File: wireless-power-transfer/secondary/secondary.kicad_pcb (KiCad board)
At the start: 2 copper layers, 100 x 67 mm, 9 parts, among them J1 Screw_Terminal_1x02, J2 Screw_Terminal_1x02, U1 LM7812CT

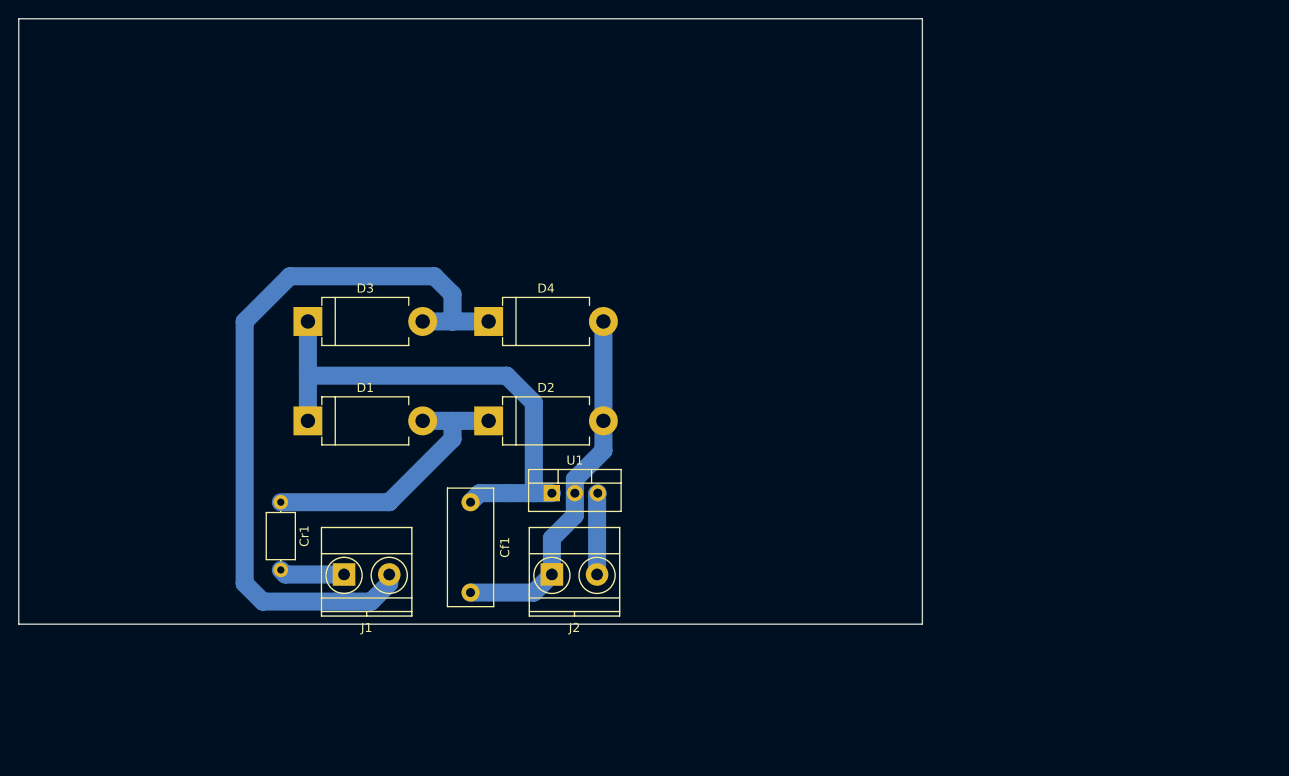
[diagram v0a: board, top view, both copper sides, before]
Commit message: Added pcb with tank and filter of the primary, some logos and other minor changes.
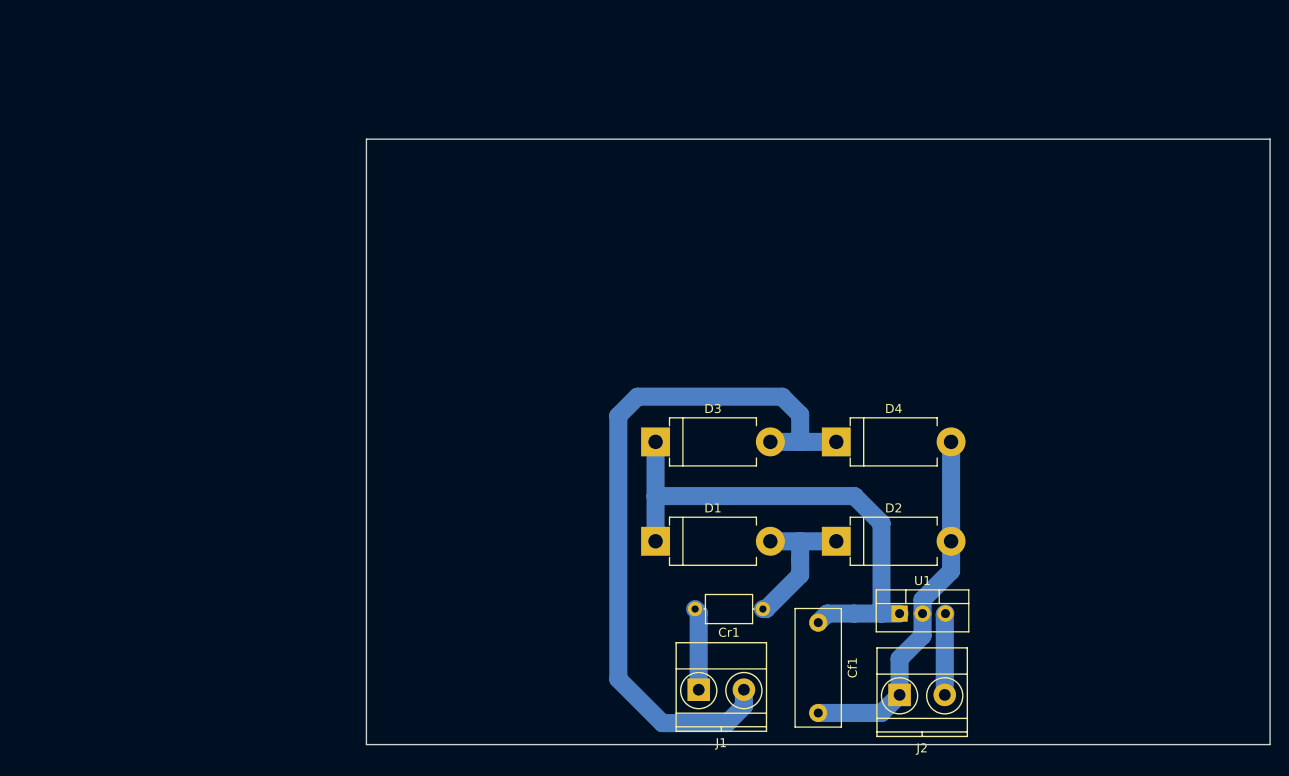
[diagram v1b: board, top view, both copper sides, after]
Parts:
- moved Cr1 54.6 mm to (132.3, 98.8), turned to 180 degrees
- moved J1 41.3 mm to (125.2, 107.8)
- moved Cf1 40.7 mm to (138.5, 100.3)
- moved D1 40.7 mm to (120.5, 91.3)
- moved D2 40.7 mm to (140.5, 91.3)
- moved D3 40.7 mm to (120.5, 80.3)
- moved D4 40.7 mm to (140.5, 80.3)
- moved J2 40.7 mm to (147.5, 108.3)
- moved U1 40.7 mm to (147.5, 99.3)
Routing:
- net Net-(Cr1-Pad1): track 31.2 -> 16.7 mm
- net Net-(D3-Pad2): track 83.9 -> 79.8 mm
- net Net-(Cr1-Pad2): track 7.21 -> 9.09 mm

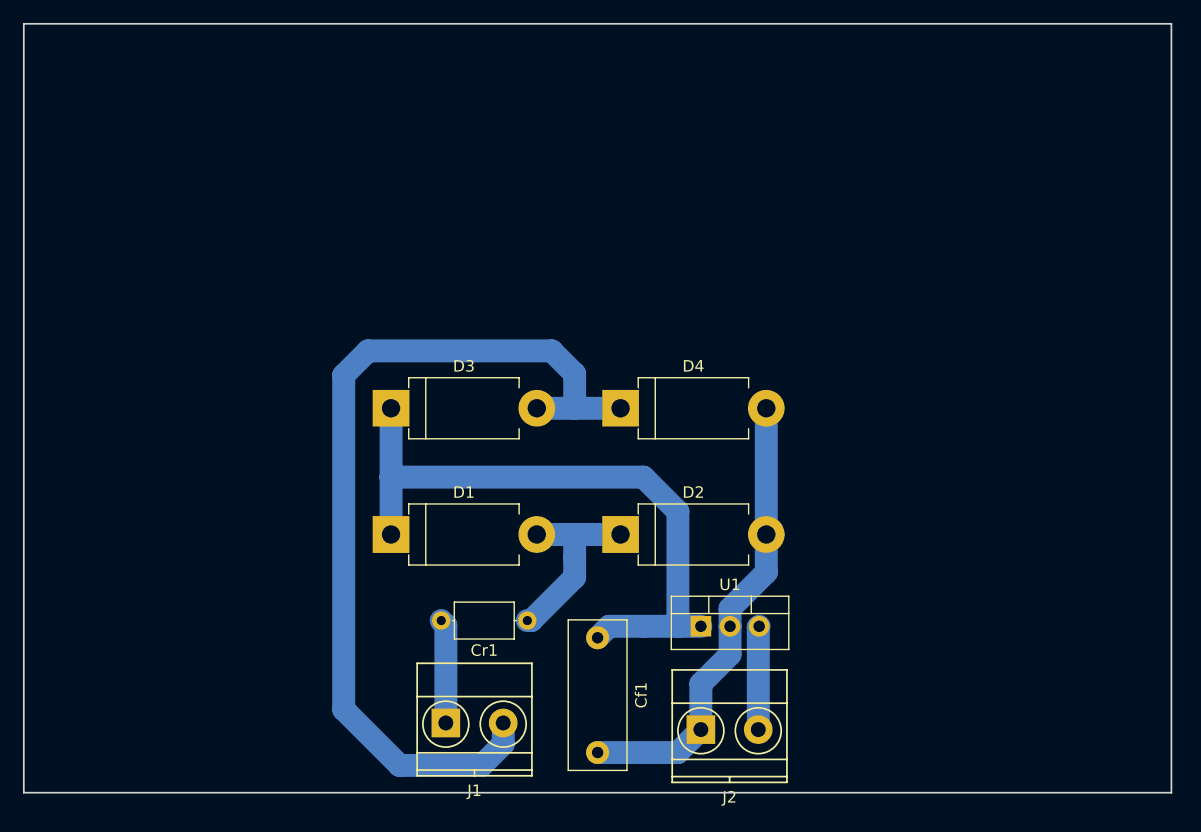
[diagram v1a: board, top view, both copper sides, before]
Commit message: Modified secondary PCB for better fitting in the car.
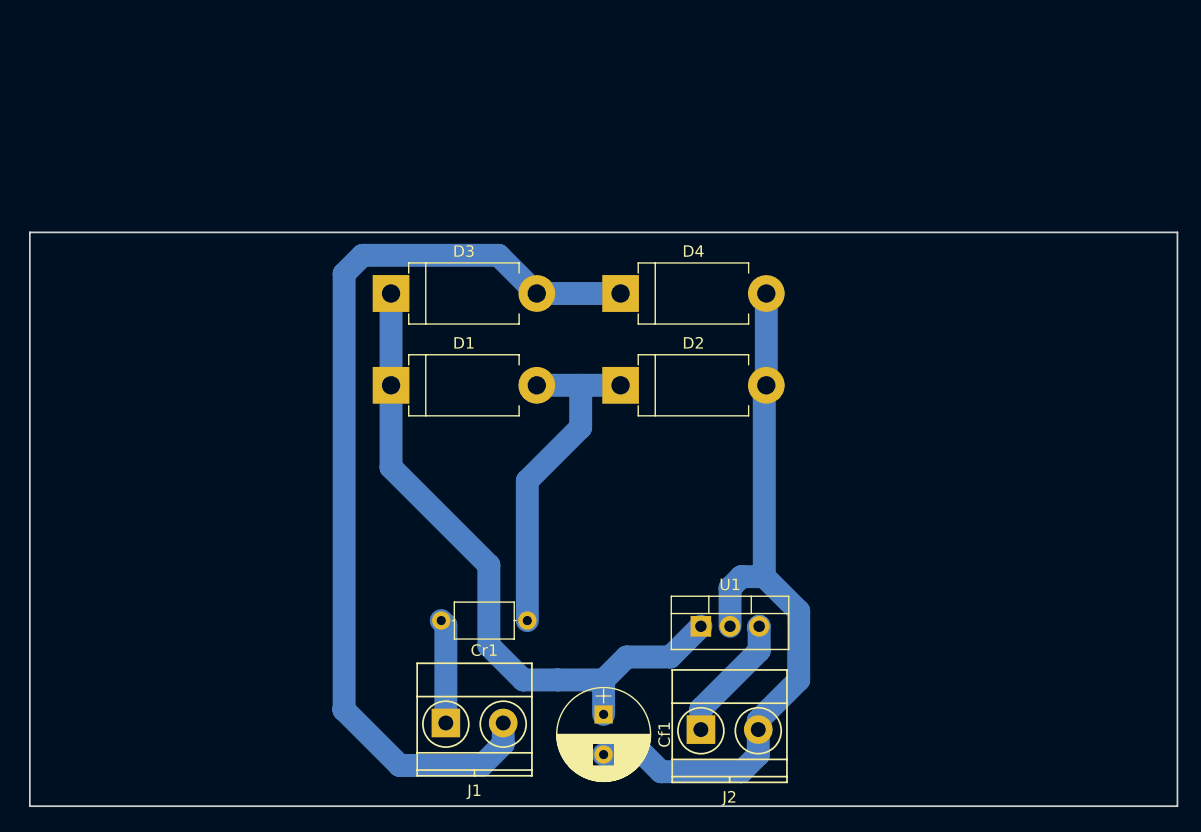
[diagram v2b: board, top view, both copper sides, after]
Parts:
- Cf1: footprint Capacitors_THT:C_Rect_L13.0mm_W5.0mm_P10.00mm_FKS3_FKP3_MKS4 -> Capacitors_THT:CP_Radial_D8.0mm_P3.50mm
- moved D1 13.0 mm to (120.5, 78.3)
- moved D2 13.0 mm to (140.5, 78.3)
- moved D3 10.0 mm to (120.5, 70.3)
- moved D4 10.0 mm to (140.5, 70.3)
- moved Cf1 6.70 mm to (139.0, 107.0)
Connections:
- J2 pad 1: Net-(Cf1-Pad2) -> Net-(J2-Pad1)
- J2 pad 2: Net-(J2-Pad2) -> Net-(Cf1-Pad2)
- U1 pad 3: Net-(J2-Pad2) -> Net-(J2-Pad1)
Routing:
- net Net-(Cf1-Pad2): track 40.2 -> 64.5 mm
- net Net-(Cr1-Pad1): track 16.7 -> 29.7 mm
- net Net-(J2-Pad1): track 0.00 -> 11.2 mm
- net Net-(J2-Pad2): track 9.15 -> 0.00 mm
- net Net-(D3-Pad2): track 79.8 -> 82.7 mm
- net Net-(Cf1-Pad1): track 56.7 -> 58.9 mm
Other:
- board size 100 x 67 mm -> 100 x 50 mm

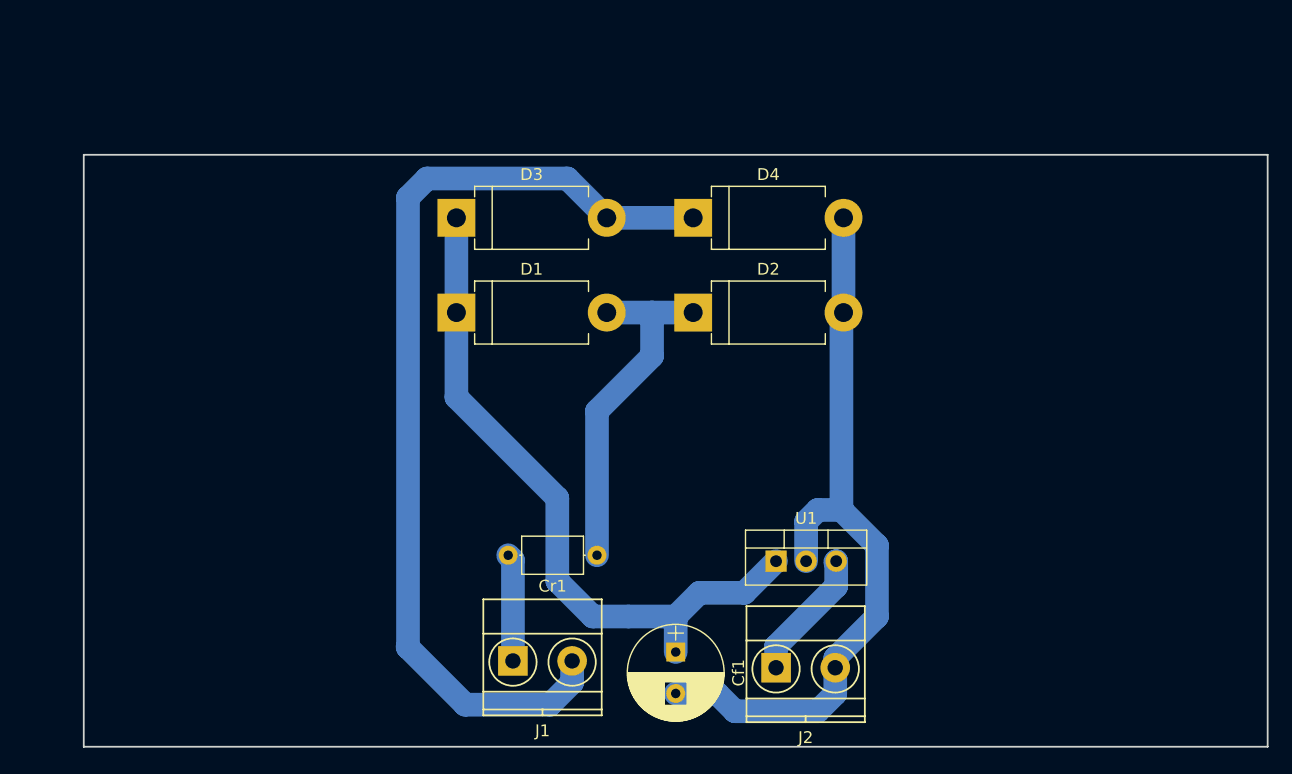
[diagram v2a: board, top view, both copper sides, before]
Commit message: modified pad sizes and secondary PCB layout.
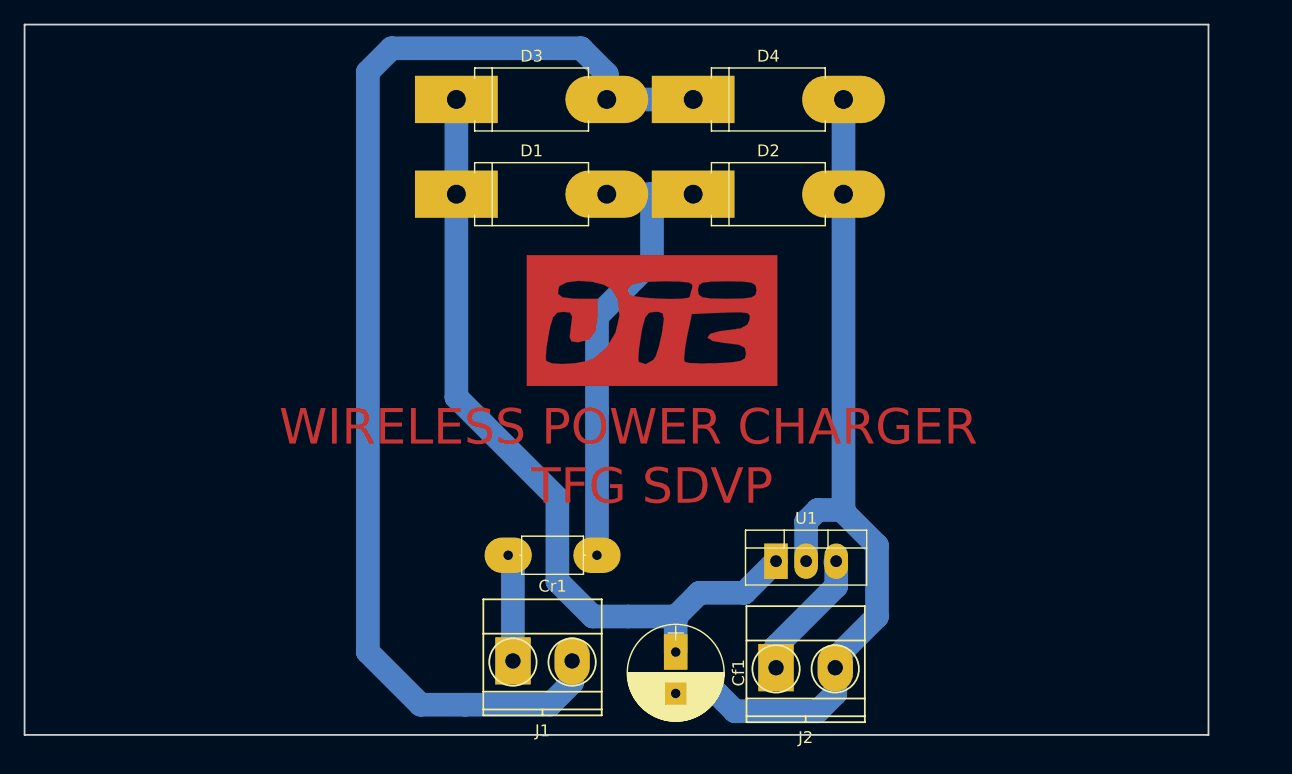
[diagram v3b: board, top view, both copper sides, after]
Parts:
- added G***: LOGO, componentes:DTE, F.Cu at (137.0, 79.0)
- moved D1 10.0 mm to (120.5, 68.3)
- moved D2 10.0 mm to (140.5, 68.3)
- moved D3 10.0 mm to (120.5, 60.3)
- moved D4 10.0 mm to (140.5, 60.3)
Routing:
- net Net-(D3-Pad2): track 82.7 -> 102.0 mm
- net Net-(Cf1-Pad2): track 64.5 -> 74.8 mm
- net Net-(Cr1-Pad1): track 29.7 -> 39.7 mm
- net Net-(Cf1-Pad1): track 58.9 -> 68.9 mm
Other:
- board size 100 x 50 mm -> 100 x 60 mm
- board text added: "TFG SDVP"
- board text added: "WIRELESS POWER CHARGER"
